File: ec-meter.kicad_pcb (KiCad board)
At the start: 2 copper layers, 46.5 x 56.5 mm, 41 parts, among them P1 Probe, P2 V+, P3 OUT, P4 V-, U1 LM324, U2 LM324

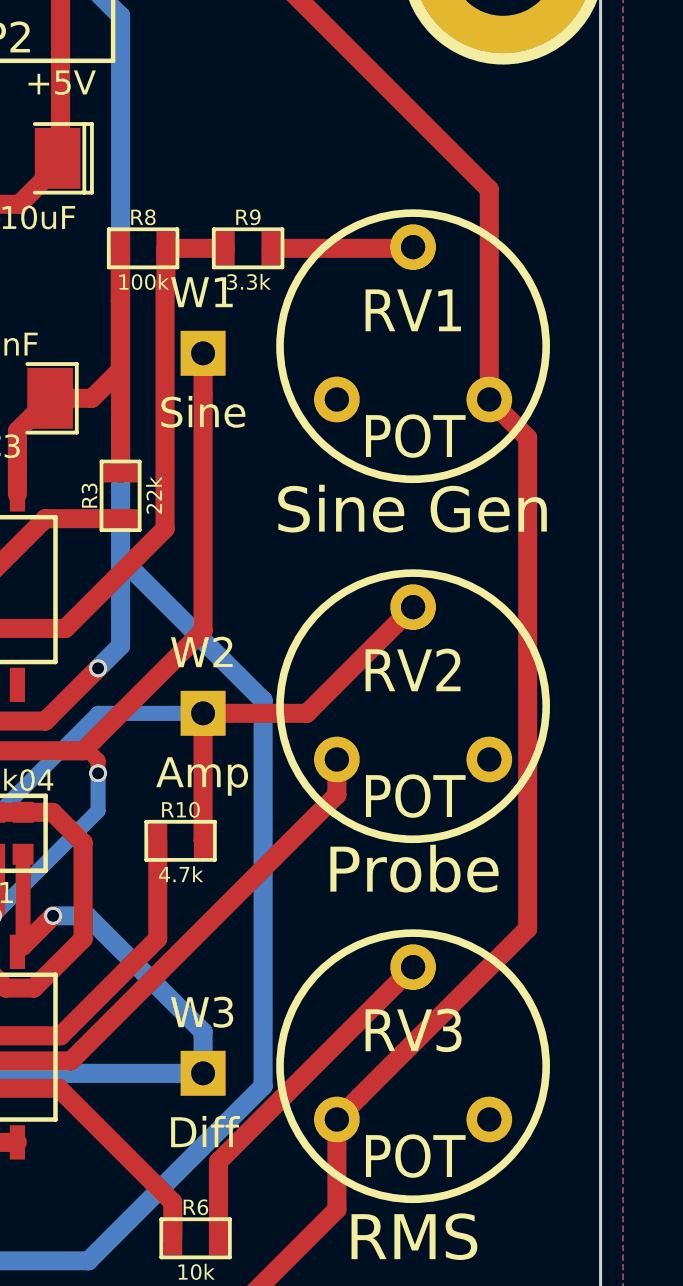
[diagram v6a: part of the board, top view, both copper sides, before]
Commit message: Changed direction of RV1
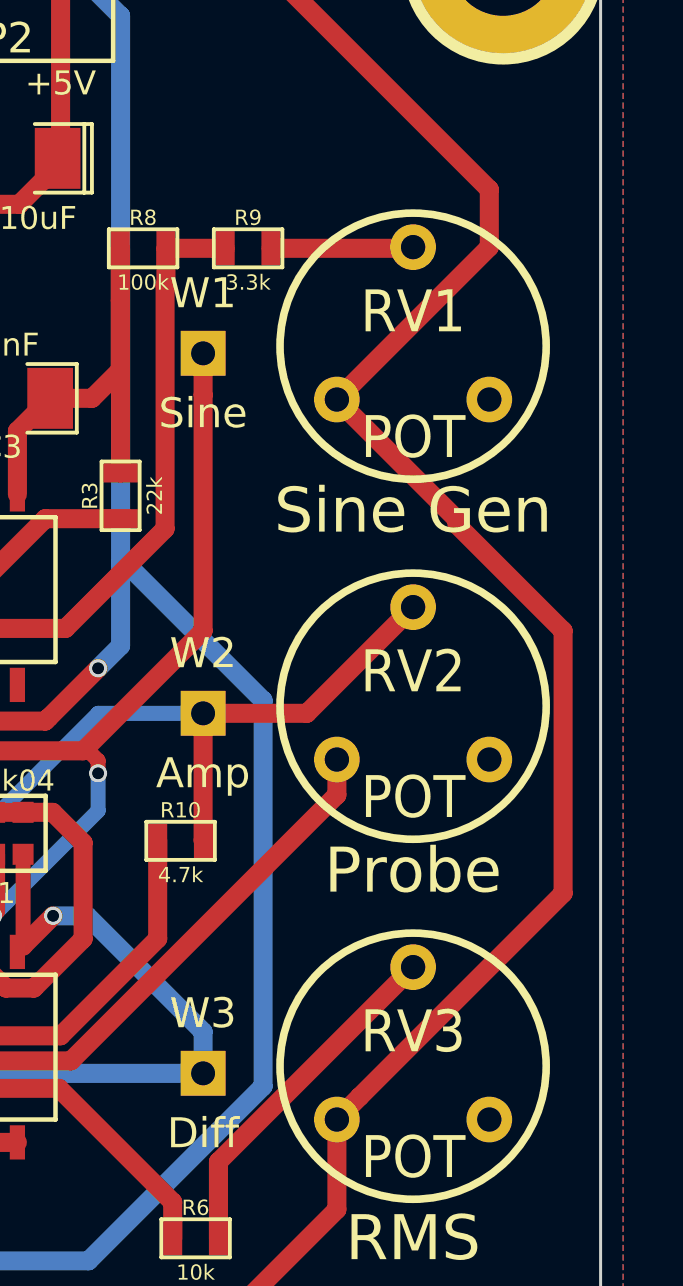
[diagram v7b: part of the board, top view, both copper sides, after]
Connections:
- RV1 pad 1: Net-(RV1-Pad1) -> GND
- RV1 pad 3: GND -> Net-(RV1-Pad3)
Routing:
- net GND: track 236.7 -> 241.8 mm
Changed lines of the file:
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@@
     (links 69)
     (no_connects 0)
-    (area 22.899999 20.899999 74.100001 81.100001)
+    (area 26.699999 21.699999 73.300001 78.300001)
     (thickness 1.6)
     (drawings 23)
-    (tracks 267)
+    (tracks 270)
     (zones 0)
     (modules 41)
@@
   (net 24 "Net-(RN1-Pad5)")
   (net 25 "Net-(RN1-Pad7)")
-  (net 26 "Net-(RV1-Pad1)")
-  (net 27 "Net-(RV2-Pad3)")
-  (net 28 "Net-(RV3-Pad3)")
+  (net 26 "Net-(RV2-Pad3)")
+  (net 27 "Net-(RV3-Pad3)")
+  (net 28 "Net-(RV1-Pad3)")
   (net_class Default "This is the default net class."
     (clearance 0.2)
@@
     (add_net "Net-(RN1-Pad5)")
     (add_net "Net-(RN1-Pad7)")
-    (add_net "Net-(RV1-Pad1)")
+    (add_net "Net-(RV1-Pad3)")
     (add_net "Net-(RV2-Pad3)")
     (add_net "Net-(RV3-Pad3)")
@@
     (fp_circle (center 0 0.762) (end 4.318 1.778) (layer F.SilkS) (width 0.254))
     (pad 1 thru_hole circle (at -2.54 2.54) (size 1.524 1.524) (drill 0.8128) (layers *.Cu *.Mask F.SilkS)
-      (net 26 "Net-(RV1-Pad1)"))
+      (net 1 GND))
     (pad 2 thru_hole circle (at 0 -2.54) (size 1.524 1.524) (drill 0.8128) (layers *.Cu *.Mask F.SilkS)
       (net 19 "Net-(R9-Pad2)"))
     (pad 3 thru_hole circle (at 2.54 2.54) (size 1.524 1.524) (drill 0.8128) (layers *.Cu *.Mask F.SilkS)
-      (net 1 GND))
+      (net 28 "Net-(RV1-Pad3)"))
     (model discret/adjustable_rx2.wrl
       (at (xyz 0 0 0))
@@
       (net 21 AmpOut))
     (pad 3 thru_hole circle (at 2.54 2.54) (size 1.524 1.524) (drill 0.8128) (layers *.Cu *.Mask F.SilkS)
-      (net 27 "Net-(RV2-Pad3)"))
+      (net 26 "Net-(RV2-Pad3)"))
     (model discret/adjustable_rx2.wrl
       (at (xyz 0 0 0))
@@
       (net 17 "Net-(R6-Pad2)"))
     (pad 3 thru_hole circle (at 2.54 2.54) (size 1.524 1.524) (drill 0.8128) (layers *.Cu *.Mask F.SilkS)
-      (net 28 "Net-(RV3-Pad3)"))
+      (net 27 "Net-(RV3-Pad3)"))
     (model discret/adjustable_rx2.wrl
       (at (xyz 0 0 0))
@@
   (gr_line (start 74 50) (end 23 50) (angle 90) (layer Cmts.User) (width 0.2))
   (gr_line (start 50 21) (end 50 81) (angle 90) (layer Cmts.User) (width 0.2))
+  (segment (start 64.46 39.54) (end 68.468169 43.548169) (width 0.635) (layer F.Cu) (net 1))
+  (segment (start 68.468169 43.548169) (end 68.468169 43.718169) (width 0.635) (layer F.Cu) (net 1))
+  (segment (start 65.221999 62.778001) (end 64.46 63.54) (width 0.635) (layer F.Cu) (net 1))
+  (segment (start 68.468169 43.718169) (end 72 47.25) (width 0.635) (layer F.Cu) (net 1))
+  (segment (start 72 47.25) (end 72 56) (width 0.635) (layer F.Cu) (net 1))
+  (segment (start 72 56) (end 65.221999 62.778001) (width 0.635) (layer F.Cu) (net 1))
+  (segment (start 69.54 32.54) (end 69.54 34.46) (width 0.635) (layer F.Cu) (net 1))
+  (segment (start 69.54 34.46) (end 64.46 39.54) (width 0.635) (layer F.Cu) (net 1))
   (segment (start 28.25 59.755) (end 28.25 49.99994) (width 0.635) (layer F.Cu) (net 1))
   (segment (start 28.25 49.99994) (end 30 48.24994) (width 0.635) (layer F.Cu) (net 1))
   (segment (start 43.775 75.026) (end 43.521 75.026) (width 0.635) (layer F.Cu) (net 1))
   (segment (start 43.521 75.026) (end 28.25 59.755) (width 0.635) (layer F.Cu) (net 1))
-  (segment (start 60.216499 23.216499) (end 69.54 32.54) (width 0.635) (layer F.Cu) (net 1))
-  (segment (start 69.54 32.54) (end 69.54 39.54) (width 0.635) (layer F.Cu) (net 1))
   (segment (start 51.74994 24.75) (end 53.283441 23.216499) (width 0.635) (layer F.Cu) (net 1))
-  (segment (start 53.283441 23.216499) (end 60.216499 23.216499) (width 0.635) (layer F.Cu) (net 1))
   (segment (start 48.25006 24.75) (end 51.74994 24.75) (width 0.635) (layer F.Cu) (net 1))
   (segment (start 48.25006 24.75) (end 48.25006 23.31316) (width 0.635) (layer F.Cu) (net 1))
@@
   (segment (start 64.46 66.54) (end 54 77) (width 0.635) (layer F.Cu) (net 1))
   (segment (start 64.46 63.54) (end 64.46 66.54) (width 0.635) (layer F.Cu) (net 1))
-  (segment (start 69.54 39.54) (end 70.819501 40.819501) (width 0.635) (layer F.Cu) (net 1))
-  (segment (start 70.819501 40.819501) (end 70.819501 57.180499) (width 0.635) (layer F.Cu) (net 1))
-  (segment (start 70.819501 57.180499) (end 65.221999 62.778001) (width 0.635) (layer F.Cu) (net 1))
-  (segment (start 65.221999 62.778001) (end 64.46 63.54) (width 0.635) (layer F.Cu) (net 1))
   (segment (start 50.25 54.25) (end 36.00006 54.25) (width 0.5) (layer B.Cu) (net 1))
   (segment (start 36.00006 54.25) (end 30 48.24994) (width 0.5) (layer B.Cu) (net 1))
@@
   (segment (start 51.74994 24.75) (end 51.74994 31.40094) (width 0.635) (layer F.Cu) (net 1))
   (segment (start 51.74994 31.40094) (end 51.849 31.5) (width 0.635) (layer F.Cu) (net 1))
+  (segment (start 60.216499 23.216499) (end 69.54 32.54) (width 0.635) (layer F.Cu) (net 1))
+  (segment (start 53.283441 23.216499) (end 60.216499 23.216499) (width 0.635) (layer F.Cu) (net 1))
   (segment (start 47.796512 43.9085) (end 48.73 43.9085) (width 0.635) (layer F.Cu) (net 2))
   (segment (start 46.373988 44.626012) (end 47.203873 44.626012) (width 0.635) (layer F.Cu) (net 2))

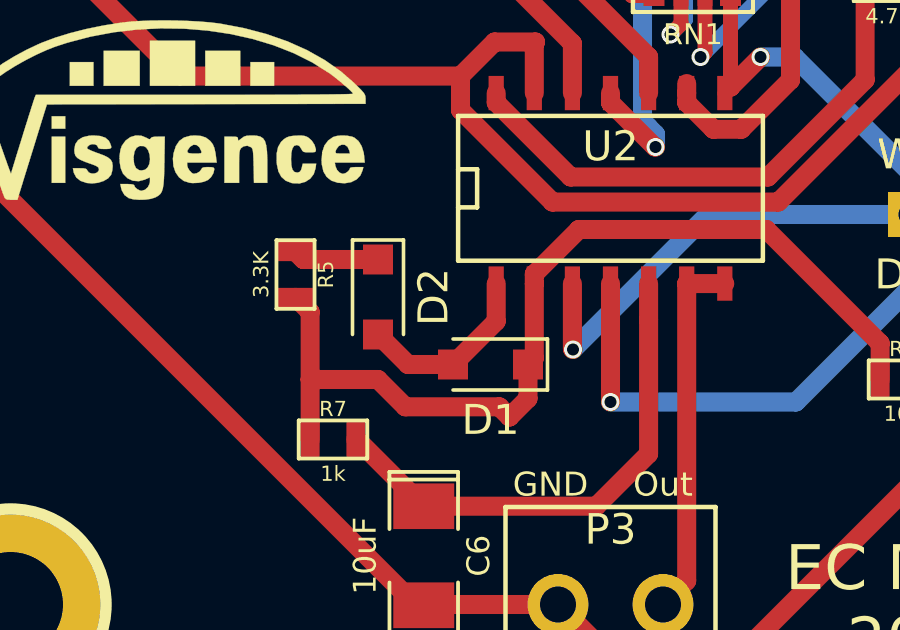
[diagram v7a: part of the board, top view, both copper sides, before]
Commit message: Changed diode to reflowable one
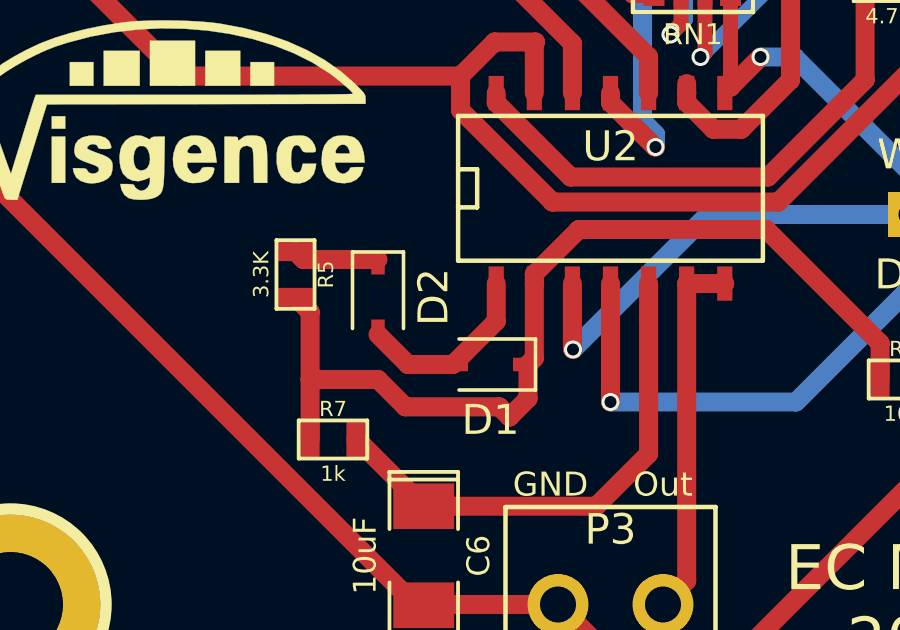
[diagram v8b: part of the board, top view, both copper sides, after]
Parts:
- D1, D2: footprint Diodes_SMD:D_SOD-323_HandSoldering -> Diodes_SMD:D_SOD-323
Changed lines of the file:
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@@
-    )
-  )
-  (module Diodes_SMD:D_SOD-323_HandSoldering (layer F.Cu)
-    (at 46 67 180)
-    (descr SOD-323)
-    (tags SOD-323)
-    (attr smd)
-    (fp_text reference D1 (at 0 -1.85 180) (layer F.SilkS)
-      (effects (font (size 1 1) (thickness 0.15)))
-    )
-    (fp_text value D (at 0.1 1.9 180) (layer F.Fab) hide
-      (effects (font (size 1 1) (thickness 0.15)))
-    )
-    (fp_line (start -1.9 -0.85) (end -1.9 0.85) (layer F.SilkS) (width 0.12))
-    (fp_line (start 0.2 0) (end 0.45 0) (layer F.Fab) (width 0.1))
-    (fp_line (start 0.2 0.35) (end -0.3 0) (layer F.Fab) (width 0.1))
-    (fp_line (start 0.2 -0.35) (end 0.2 0.35) (layer F.Fab) (width 0.1))
-    (fp_line (start -0.3 0) (end 0.2 -0.35) (layer F.Fab) (width 0.1))
-    (fp_line (start -0.3 0) (end -0.5 0) (layer F.Fab) (width 0.1))
-    (fp_line (start -0.3 -0.35) (end -0.3 0.35) (layer F.Fab) (width 0.1))
-    (fp_line (start -0.9 0.7) (end -0.9 -0.7) (layer F.Fab) (width 0.1))
-    (fp_line (start 0.9 0.7) (end -0.9 0.7) (layer F.Fab) (width 0.1))
-    (fp_line (start 0.9 -0.7) (end 0.9 0.7) (layer F.Fab) (width 0.1))
-    (fp_line (start -0.9 -0.7) (end 0.9 -0.7) (layer F.Fab) (width 0.1))
-    (fp_line (start -2 -0.95) (end 2 -0.95) (layer F.CrtYd) (width 0.05))
-    (fp_line (start 2 -0.95) (end 2 0.95) (layer F.CrtYd) (width 0.05))
-    (fp_line (start -2 0.95) (end 2 0.95) (layer F.CrtYd) (width 0.05))
-    (fp_line (start -2 -0.95) (end -2 0.95) (layer F.CrtYd) (width 0.05))
-    (fp_line (start -1.9 0.85) (end 1.25 0.85) (layer F.SilkS) (width 0.12))
-    (fp_line (start -1.9 -0.85) (end 1.25 -0.85) (layer F.SilkS) (width 0.12))
-    (pad 1 smd rect (at -1.25 0 180) (size 1 1) (layers F.Cu F.Paste F.Mask)
-      (net 10 "Net-(D1-Pad1)"))
-    (pad 2 smd rect (at 1.25 0 180) (size 1 1) (layers F.Cu F.Paste F.Mask)
-      (net 11 "Net-(D1-Pad2)"))
-    (model Diodes_SMD.3dshapes/D_SOD-323.wrl
-      (at (xyz 0 0 0))
-      (scale (xyz 1 1 1))
-      (rotate (xyz 0 0 180))
-    )
-  )
-  (module Diodes_SMD:D_SOD-323_HandSoldering (layer F.Cu)
-    (at 42.25 64.75 270)
-    (descr SOD-323)
-    (tags SOD-323)
-    (attr smd)
-    (fp_text reference D2 (at 0 -1.85 270) (layer F.SilkS)
-      (effects (font (size 1 1) (thickness 0.15)))
-    )
-    (fp_text value D (at 0.1 1.9 270) (layer F.Fab) hide
-      (effects (font (size 1 1) (thickness 0.15)))
-    )
-    (fp_line (start -1.9 -0.85) (end -1.9 0.85) (layer F.SilkS) (width 0.12))
-    (fp_line (start 0.2 0) (end 0.45 0) (layer F.Fab) (width 0.1))
-    (fp_line (start 0.2 0.35) (end -0.3 0) (layer F.Fab) (width 0.1))
-    (fp_line (start 0.2 -0.35) (end 0.2 0.35) (layer F.Fab) (width 0.1))
-    (fp_line (start -0.3 0) (end 0.2 -0.35) (layer F.Fab) (width 0.1))
-    (fp_line (start -0.3 0) (end -0.5 0) (layer F.Fab) (width 0.1))
-    (fp_line (start -0.3 -0.35) (end -0.3 0.35) (layer F.Fab) (width 0.1))
-    (fp_line (start -0.9 0.7) (end -0.9 -0.7) (layer F.Fab) (width 0.1))
-    (fp_line (start 0.9 0.7) (end -0.9 0.7) (layer F.Fab) (width 0.1))
-    (fp_line (start 0.9 -0.7) (end 0.9 0.7) (layer F.Fab) (width 0.1))
-    (fp_line (start -0.9 -0.7) (end 0.9 -0.7) (layer F.Fab) (width 0.1))
-    (fp_line (start -2 -0.95) (end 2 -0.95) (layer F.CrtYd) (width 0.05))
-    (fp_line (start 2 -0.95) (end 2 0.95) (layer F.CrtYd) (width 0.05))
-    (fp_line (start -2 0.95) (end 2 0.95) (layer F.CrtYd) (width 0.05))
-    (fp_line (start -2 -0.95) (end -2 0.95) (layer F.CrtYd) (width 0.05))
-    (fp_line (start -1.9 0.85) (end 1.25 0.85) (layer F.SilkS) (width 0.12))
-    (fp_line (start -1.9 -0.85) (end 1.25 -0.85) (layer F.SilkS) (width 0.12))
-    (pad 1 smd rect (at -1.25 0 270) (size 1 1) (layers F.Cu F.Paste F.Mask)
-      (net 12 "Net-(D2-Pad1)"))
-    (pad 2 smd rect (at 1.25 0 270) (size 1 1) (layers F.Cu F.Paste F.Mask)
-      (net 11 "Net-(D1-Pad2)"))
-    (model Diodes_SMD.3dshapes/D_SOD-323.wrl
-      (at (xyz 0 0 0))
-      (scale (xyz 1 1 1))
-      (rotate (xyz 0 0 180))
     )
   )
@@
       (xy 6.821715 1.524)) (layer B.SilkS) (width 0.01))
   )
+  (module Diodes_SMD:D_SOD-323 (layer F.Cu)
+    (at 46 67 180)
+    (descr SOD-323)
+    (tags SOD-323)
+    (attr smd)
+    (fp_text reference D1 (at 0 -1.85 180) (layer F.SilkS)
+      (effects (font (size 1 1) (thickness 0.15)))
+    )
+    (fp_text value D (at 0.1 1.9 180) (layer F.Fab)
+      (effects (font (size 1 1) (thickness 0.15)))
+    )
+    (fp_line (start -1.5 -0.85) (end -1.5 0.85) (layer F.SilkS) (width 0.12))
+    (fp_line (start 0.2 0) (end 0.45 0) (layer F.Fab) (width 0.1))
+    (fp_line (start 0.2 0.35) (end -0.3 0) (layer F.Fab) (width 0.1))
+    (fp_line (start 0.2 -0.35) (end 0.2 0.35) (layer F.Fab) (width 0.1))
+    (fp_line (start -0.3 0) (end 0.2 -0.35) (layer F.Fab) (width 0.1))
+    (fp_line (start -0.3 0) (end -0.5 0) (layer F.Fab) (width 0.1))
+    (fp_line (start -0.3 -0.35) (end -0.3 0.35) (layer F.Fab) (width 0.1))
+    (fp_line (start -0.9 0.7) (end -0.9 -0.7) (layer F.Fab) (width 0.1))
+    (fp_line (start 0.9 0.7) (end -0.9 0.7) (layer F.Fab) (width 0.1))
+    (fp_line (start 0.9 -0.7) (end 0.9 0.7) (layer F.Fab) (width 0.1))
+    (fp_line (start -0.9 -0.7) (end 0.9 -0.7) (layer F.Fab) (width 0.1))
+    (fp_line (start -1.6 -0.95) (end 1.6 -0.95) (layer F.CrtYd) (width 0.05))
+    (fp_line (start 1.6 -0.95) (end 1.6 0.95) (layer F.CrtYd) (width 0.05))
+    (fp_line (start -1.6 0.95) (end 1.6 0.95) (layer F.CrtYd) (width 0.05))
+    (fp_line (start -1.6 -0.95) (end -1.6 0.95) (layer F.CrtYd) (width 0.05))
+    (fp_line (start -1.5 0.85) (end 1.05 0.85) (layer F.SilkS) (width 0.12))
+    (fp_line (start -1.5 -0.85) (end 1.05 -0.85) (layer F.SilkS) (width 0.12))
+    (pad 1 smd rect (at -1.05 0 180) (size 0.6 0.45) (layers F.Cu F.Paste F.Mask)
+      (net 10 "Net-(D1-Pad1)"))
+    (pad 2 smd rect (at 1.05 0 180) (size 0.6 0.45) (layers F.Cu F.Paste F.Mask)
+      (net 11 "Net-(D1-Pad2)"))
+    (model Diodes_SMD.3dshapes/D_SOD-323.wrl
+      (at (xyz 0 0 0))
+      (scale (xyz 1 1 1))
+      (rotate (xyz 0 0 180))
+    )
+  )
+  (module Diodes_SMD:D_SOD-323 (layer F.Cu)
+    (at 42.25 64.75 270)
+    (descr SOD-323)
+    (tags SOD-323)
+    (attr smd)
+    (fp_text reference D2 (at 0 -1.85 270) (layer F.SilkS)
+      (effects (font (size 1 1) (thickness 0.15)))
+    )
+    (fp_text value D (at 0.1 1.9 270) (layer F.Fab)
+      (effects (font (size 1 1) (thickness 0.15)))
+    )
+    (fp_line (start -1.5 -0.85) (end -1.5 0.85) (layer F.SilkS) (width 0.12))
+    (fp_line (start 0.2 0) (end 0.45 0) (layer F.Fab) (width 0.1))
+    (fp_line (start 0.2 0.35) (end -0.3 0) (layer F.Fab) (width 0.1))
+    (fp_line (start 0.2 -0.35) (end 0.2 0.35) (layer F.Fab) (width 0.1))
+    (fp_line (start -0.3 0) (end 0.2 -0.35) (layer F.Fab) (width 0.1))
+    (fp_line (start -0.3 0) (end -0.5 0) (layer F.Fab) (width 0.1))
+    (fp_line (start -0.3 -0.35) (end -0.3 0.35) (layer F.Fab) (width 0.1))
+    (fp_line (start -0.9 0.7) (end -0.9 -0.7) (layer F.Fab) (width 0.1))
+    (fp_line (start 0.9 0.7) (end -0.9 0.7) (layer F.Fab) (width 0.1))
+    (fp_line (start 0.9 -0.7) (end 0.9 0.7) (layer F.Fab) (width 0.1))
+    (fp_line (start -0.9 -0.7) (end 0.9 -0.7) (layer F.Fab) (width 0.1))
+    (fp_line (start -1.6 -0.95) (end 1.6 -0.95) (layer F.CrtYd) (width 0.05))
+    (fp_line (start 1.6 -0.95) (end 1.6 0.95) (layer F.CrtYd) (width 0.05))
+    (fp_line (start -1.6 0.95) (end 1.6 0.95) (layer F.CrtYd) (width 0.05))
+    (fp_line (start -1.6 -0.95) (end -1.6 0.95) (layer F.CrtYd) (width 0.05))
+    (fp_line (start -1.5 0.85) (end 1.05 0.85) (layer F.SilkS) (width 0.12))
+    (fp_line (start -1.5 -0.85) (end 1.05 -0.85) (layer F.SilkS) (width 0.12))
+    (pad 1 smd rect (at -1.05 0 270) (size 0.6 0.45) (layers F.Cu F.Paste F.Mask)
+      (net 12 "Net-(D2-Pad1)"))
+    (pad 2 smd rect (at 1.05 0 270) (size 0.6 0.45) (layers F.Cu F.Paste F.Mask)
+      (net 11 "Net-(D1-Pad2)"))
+    (model Diodes_SMD.3dshapes/D_SOD-323.wrl
+      (at (xyz 0 0 0))
+      (scale (xyz 1 1 1))
+      (rotate (xyz 0 0 180))
+    )
+  )
   (gr_text "EC Meter\n2017" (at 60.5 75) (layer F.SilkS)
